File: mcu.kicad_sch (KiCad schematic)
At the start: 37 parts, among them J2 USB_C_Receptacle_USB2.0_16P, J3 Conn_01x06_Socket, SW1 SW_Push, SW2 SW_Push, SW3 SW_Rotary_1x4_MP, SW4 SW_Push_Shielded, SW5 SW_Push_Shielded, SW6 SW_Push_Shielded, SW7 SW_Push_Shielded, U1 STM32H743VITx, U6 MX25L25645GM2I

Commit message: Power Supply Speccing, IMU, Eyeballs
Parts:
- D1, D2: value LED_Filled -> QBLP601-R5-2897
- R15, R16: value R_US -> 240
- R17, R18, R19, R20: value R_US -> 5k
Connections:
- net ACCEL_CS: now also U1.32 (PC4)
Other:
- note added: "Add capacitors for hardware debounce!"
- note removed: "Use 25MHz crystal, best choice for STM32H743"
- moved on the sheet: BZ1, C1, C2, C22, C3, C4, C5, C6, C8, C9, D1, D2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

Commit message: Release Candidate 1
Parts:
- removed SW1, SW2: SW_Push, symbol Switch:SW_Push
- added C24: 4.7u, Capacitor_SMD:C_0805_2012Metric, symbol Device:C
- added D6, D9: CLV1L-FKB, LED_SMD:LED_Cree-PLCC4_3.2x2.8mm_CCW, symbol LED:CLV1L-FKB
- added D7, D8: QBLP601-R5-2897, LED_SMD:LED_0603_1608Metric, symbol Device:LED_Filled
- added J6: Conn_02x02_Counter_Clockwise, Connector_PinHeader_1.00mm:PinHeader_2x02_P1.00mm_Vertical, symbol Connector_Generic:Conn_02x02_Counter_Clockwise
- added Q3: DMG2302U, Package_TO_SOT_SMD:SOT-23, symbol Transistor_FET:DMG2302U
- added R23, R24, R30, R31: 43, Resistor_SMD:R_0805_2012Metric, symbol Device:R_US
- added R25, R29: 110, Resistor_SMD:R_0805_2012Metric, symbol Device:R_US
- added R26, R27: 240, Resistor_SMD:R_0805_2012Metric, symbol Device:R_US
- added SW1, SW2: SW_Push_Shielded, 0_airbrake_footprints:R-667766, symbol Switch:SW_Push_Shielded
- added Y1: Crystal_GND24, Crystal:Crystal_SMD_2016-4Pin_2.0x1.6mm, symbol Device:Crystal_GND24
- BZ1: footprint Buzzer_Beeper:Buzzer_TDK_PS1240P02BT_D12.2mm_H6.5mm -> 0_airbrake_footprints:CMT-322-65-SMT-TR
- C1, C2: value C -> 8p
- SW3: footprint (none) -> 0_airbrake_footprints:S-2051
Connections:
- net 3V3_MCU: now also C24.1, J6.1 (Pin_1), SW2.2
- net Buzzer_H: now also Q3.1 (G); no longer BZ1.1 (+)
- net GND: now also C24.2, D7.1 (K), D8.1 (K), J6.2 (Pin_2), Q3.2 (S), SW1.2, SW1.SH (B), SW2.SH (B), Y1.2, Y1.4
- net MCU_NRST: now also SW1.1
- net MODE_0: now also U1.81 (PD0); no longer U1.15 (PC0)
- net MODE_1: now also U1.82 (PD1); no longer U1.16 (PC1)
- net MODE_2: now also U1.83 (PD2); no longer U1.17 (PC2_C)
- net MODE_3: now also U1.84 (PD3); no longer U1.18 (PC3_C)
- net VBUS_DETECT: now also U1.51 (PB12)
- net XTAL_0: now also Y1.3
- net XTAL_1: now also Y1.1
- net STATUS1: now reaches U1.34 (PB0)
- net STATUS1: now also R27.1
- net STATUS_POW: now reaches U1.35 (PB1)
- net STATUS_POW: now also R26.1
- net BAT_OK_MCU: now reaches U1.40 (PE10)
- net STATUS0_R: now reaches U1.41 (PE11)
- net STATUS0_R: now also R25.2
- net STATUS0_G: now reaches U1.43 (PE13)
- net STATUS0_G: now also R24.2
- net STATUS0_B: now reaches U1.44 (PE14)
- net STATUS0_B: now also R23.2
- net GPS_TP: now reaches U1.47 (PB11)
- net SERVO_EN: now reaches U1.91 (PB5)
- net at R1.2, U1.94 (BOOT0): now also SW2.1
- net SERVO_SIG: now reaches U1.95 (PB8)
- net Buzzer_L: no longer names the net of U1.38 (PE8)
- net Buzzer_L: no longer BZ1.2 (-)
- net MCU_I2C1_SCL renamed EXT_I2C1_SCL
- net EXT_I2C1_SCL: now also J6.4 (Pin_4)
- net MCU_I2C1_SDA renamed EXT_I2C1_SDA
- net EXT_I2C1_SDA: now also J6.3 (Pin_3)
- net MCU_I2C3_SCL renamed BME680_I2C3_SCL
- net MCU_I2C3_SDA renamed BME680_I2C3_SDA
- new net: D9.2 (RK), R29.1
- new net: D9.3 (GK), R30.1
- new net: D9.4 (BK), R31.1
- new net: BZ1.2 (-), Q3.3 (D)
- new net: D8.2 (A), R27.2
- new net: D6.2 (RK), R25.1
- new net: D7.2 (A), R26.2
- new net: D6.3 (GK), R24.1
- new net: D6.4 (BK), R23.1
- new net 3V6_SWITCHING: BZ1.1 (+), D6.1 (A), D9.1 (A)
- new net STATUS1_B: R31.2, U1.17 (PC2_C)
- new net STATUS1_G: R30.2, U1.16 (PC1)
- new net STATUS1_R: R29.2, U1.15 (PC0)
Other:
- note added: "5V Tolerant!"
- note added: "External I2C"
- note added: "https://www.digikey.com/en/products/detail/cree-led/CLV1L-FKB-CJQRNQEFGBB79353/9659628"
- note removed: "Add capacitors for hardware debounce!"
- note removed: "Run buzzer on complementary PWM to make it really loud!"
- moved on the sheet: BZ1, C1, C2, SW3, SW4, SW5, SW6, SW7

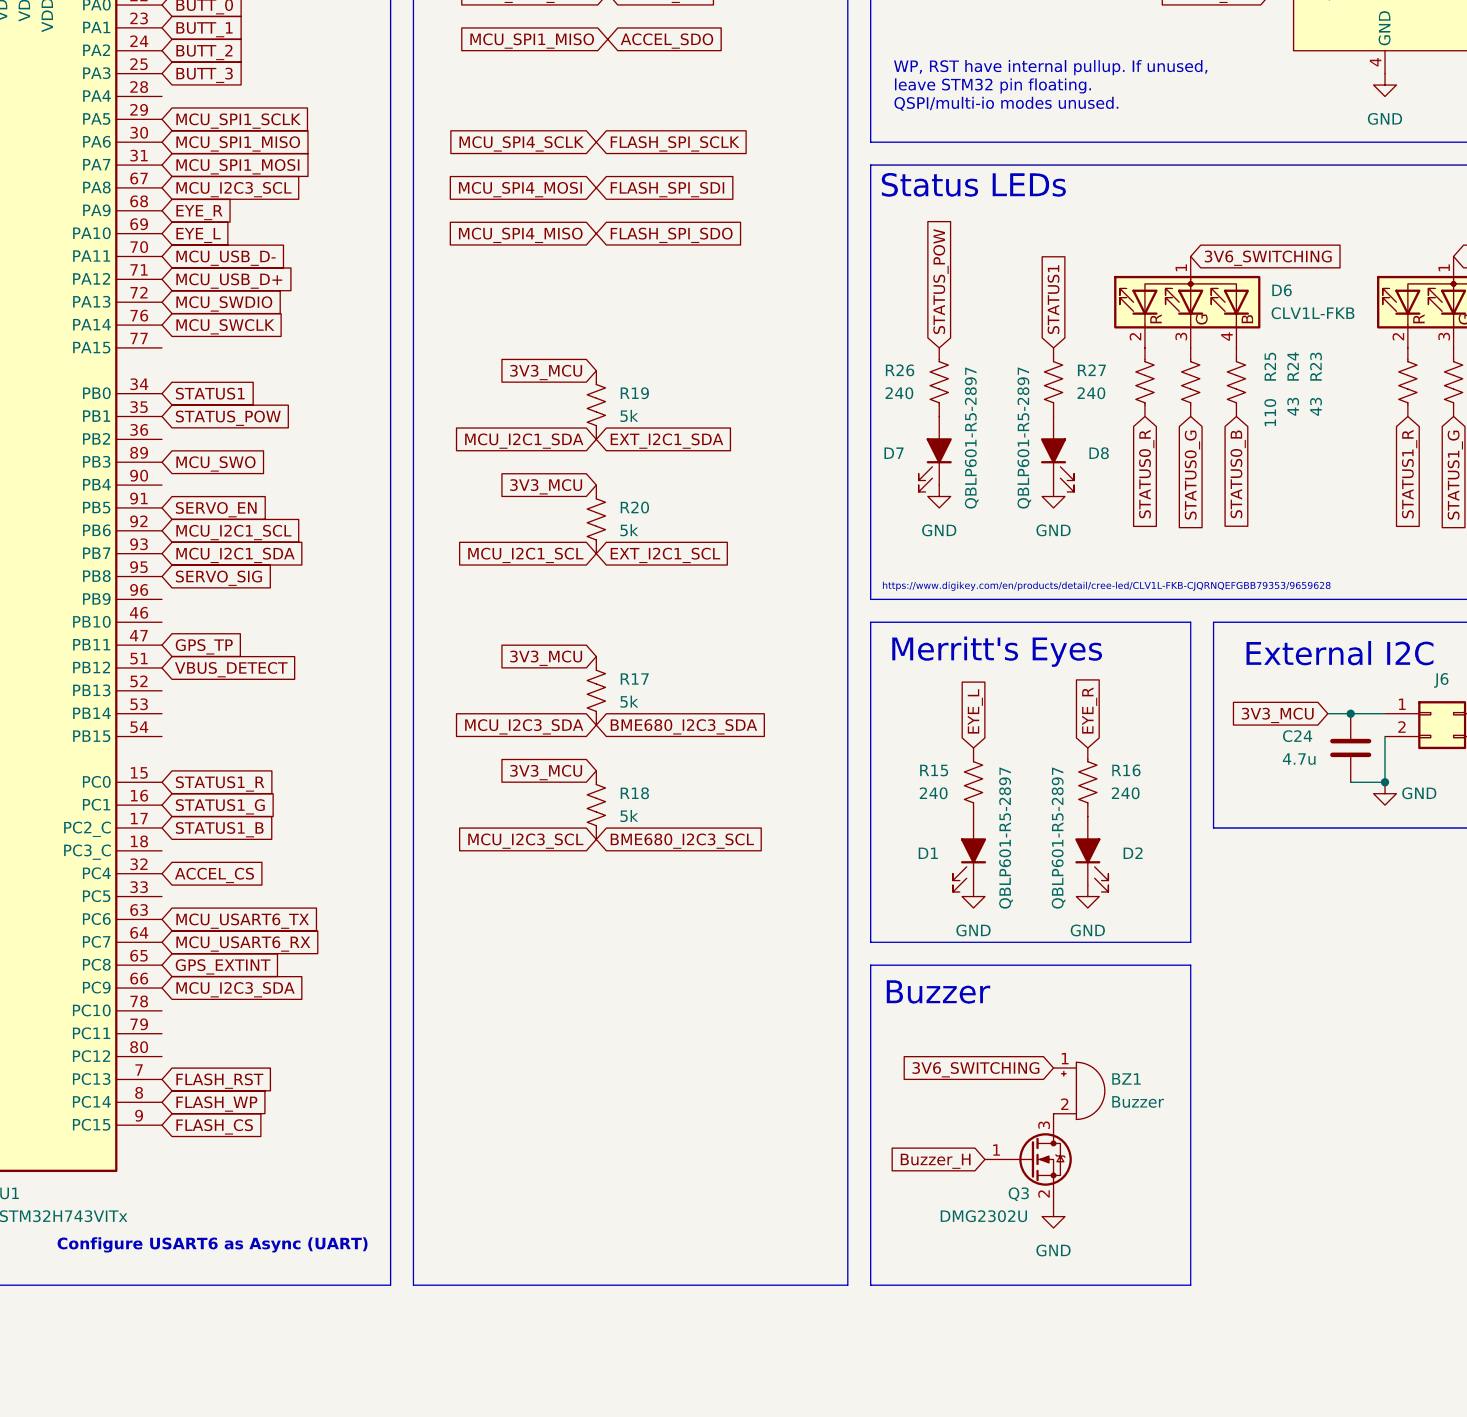
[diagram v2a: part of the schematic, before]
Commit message: Release Candidate 2
Incorporates fixes for all identified issues in the PCBR
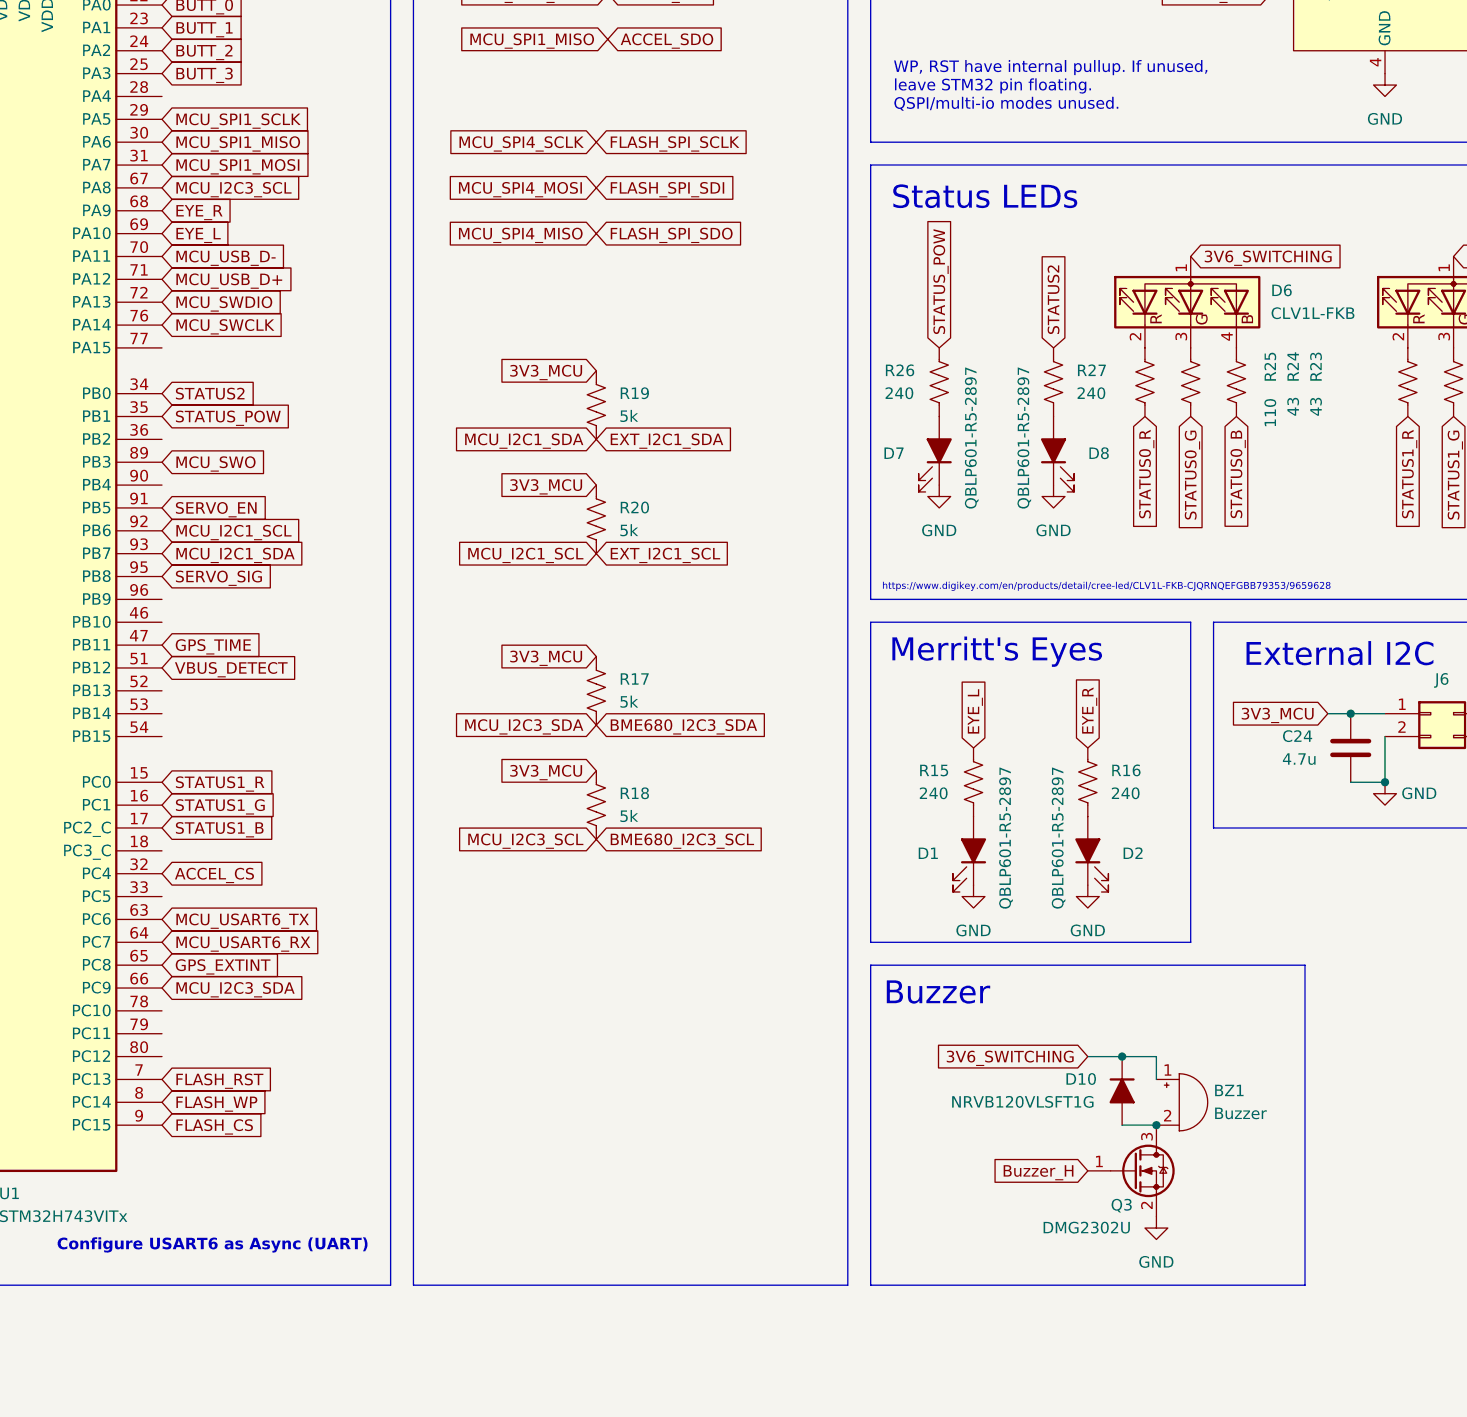
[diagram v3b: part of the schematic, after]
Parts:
- added D10: NRVB120VLSFT1G, Diode_SMD:D_SOD-123F, symbol Device:D_Filled
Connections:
- net 3V6_SWITCHING: now also D10.1 (K)
- net at BZ1.2 (-), Q3.3 (D): now also D10.2 (A)
- net GPS_TP renamed GPS_TIME
- net STATUS1 renamed STATUS2
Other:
- moved on the sheet: BZ1, Q3
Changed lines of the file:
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@@
 	)
 	(junction
+		(at 325.12 184.15)
+		(diameter 0)
+		(color 0 0 0 0)
+	)
+	(junction
 		(at 199.39 52.07)
 		(diameter 0)
 		(color 0 0 0 0)
 	)
+	(junction
+		(at 321.31 176.53)
+		(diameter 0)
+		(color 0 0 0 0)
+	)
 	(no_connect
 		(at 171.45 69.85)
@@
 	(wire
 		(pts
+			(xy 325.12 176.53) (xy 325.12 179.07)
+		)
+		(stroke
+			(width 0)
+			(type default)
+		)
+	)
+	(wire
+		(pts
 			(xy 74.93 93.98) (xy 82.55 93.98)
 		)
@@
 	(wire
 		(pts
+			(xy 321.31 184.15) (xy 325.12 184.15)
+		)
+		(stroke
+			(width 0)
+			(type default)
+		)
+	)
+	(wire
+		(pts
 			(xy 74.93 101.6) (xy 82.55 101.6)
 		)
@@
 	(wire
 		(pts
+			(xy 317.5 176.53) (xy 321.31 176.53)
+		)
+		(stroke
+			(width 0)
+			(type default)
+		)
+	)
+	(wire
+		(pts
 			(xy 346.71 138.43) (xy 350.52 138.43)
 		)
@@
 	(wire
 		(pts
+			(xy 321.31 176.53) (xy 325.12 176.53)
+		)
+		(stroke
+			(width 0)
+			(type default)
+		)
+	)
+	(wire
+		(pts
 			(xy 139.7 64.77) (xy 146.05 64.77)
 		)
@@
 	(rectangle
 		(start 293.37 166.37)
-		(end 328.93 201.93)
+		(end 341.63 201.93)
 		(stroke
 			(width 0)
@@
 	(text "Status LEDs"
 		(exclude_from_sim no)
-		(at 304.8 80.01 0)
+		(at 306.07 81.28 0)
 		(effects
 			(font
@@
 		)
 	)
-	(global_label "STATUS1"
+	(global_label "STATUS2"
 		(shape input)
 		(at 313.69 97.79 90)
@@
 		)
 	)
-	(global_label "GPS_TP"
-		(shape input)
-		(at 214.63 130.81 0)
-		(fields_autoplaced yes)
-		(effects
-			(font
-				(size 1.27 1.27)
-			)
-			(justify left)
-		)
-		(property "Intersheetrefs" "${INTERSHEET_REFS}"
-			(at 224.5699 130.81 0)
-			(effects
-				(font
-					(size 1.27 1.27)
-				)
-				(justify left)
-				(hide yes)
-			)
-		)
-	)
 	(global_label "XTAL_1"
 		(shape input)
@@
 		)
 	)
+	(global_label "GPS_TIME"
+		(shape input)
+		(at 214.63 130.81 0)
+		(fields_autoplaced yes)
+		(effects
+			(font
+				(size 1.27 1.27)
+			)
+			(justify left)
+		)
+		(property "Intersheetrefs" "${INTERSHEET_REFS}"
+			(at 226.5051 130.81 0)
+			(effects
+				(font
+					(size 1.27 1.27)
+				)
+				(justify left)
+				(hide yes)
+			)
+		)
+	)
 	(global_label "3V3_MCU"
 		(shape input)
@@
 	(global_label "3V6_SWITCHING"
 		(shape input)
-		(at 313.69 177.8 180)
+		(at 317.5 176.53 180)
 		(fields_autoplaced yes)
 		(effects
@@
 		)
 		(property "Intersheetrefs" "${INTERSHEET_REFS}"
-			(at 296.1905 177.8 0)
+			(at 300.0005 176.53 0)
 			(effects
 				(font
@@
 		)
 	)
-	(global_label "STATUS1"
+	(global_label "STATUS2"
 		(shape input)
 		(at 214.63 102.87 0)
@@
 	(global_label "Buzzer_H"
 		(shape input)
-		(at 306.07 187.96 180)
+		(at 317.5 189.23 180)
 		(fields_autoplaced yes)
 		(effects
@@
 		)
 		(property "Intersheetrefs" "${INTERSHEET_REFS}"
-			(at 294.4367 187.96 0)
+			(at 305.8667 189.23 0)
 			(effects
 				(font
@@
 	(symbol
 		(lib_id "Transistor_FET:DMG2302U")
-		(at 311.15 187.96 0)
+		(at 322.58 189.23 0)
 		(unit 1)
 		(exclude_from_sim no)
@@
 		(dnp no)
 		(property "Reference" "Q3"
-			(at 308.61 191.77 0)
+			(at 320.04 193.04 0)
 			(effects
 				(font
@@
 		)
 		(property "Value" "DMG2302U"
-			(at 300.99 194.31 0)
+			(at 312.42 195.58 0)
 			(effects
 				(font
@@
 		)
 		(property "Footprint" "Package_TO_SOT_SMD:SOT-23"
-			(at 316.23 189.865 0)
+			(at 327.66 191.135 0)
 			(effects
 				(font
@@
 		)
 		(property "Datasheet" "http://www.diodes.com/assets/Datasheets/DMG2302U.pdf"
-			(at 316.23 191.77 0)
+			(at 327.66 193.04 0)
 			(effects
 				(font
@@
 		)
 		(property "Description" "4.2A Id, 20V Vds, N-Channel MOSFET, SOT-23"
-			(at 311.15 187.96 0)
+			(at 322.58 189.23 0)
 			(effects
 				(font
@@
 	(symbol
 		(lib_id "Device:Buzzer")
-		(at 316.23 180.34 0)
+		(at 327.66 181.61 0)
 		(unit 1)
 		(exclude_from_sim no)
@@
 		(fields_autoplaced yes)
 		(property "Reference" "BZ1"
-			(at 320.04 179.0699 0)
+			(at 331.47 180.3399 0)
 			(effects
 				(font
@@
 		)
 		(property "Value" "Buzzer"
-			(at 320.04 181.6099 0)
+			(at 331.47 182.8799 0)
 			(effects
 				(font
@@
 		)
 		(property "Footprint" "0_airbrake_footprints:CMT-322-65-SMT-TR"
-			(at 315.595 177.8 90)
+			(at 327.025 179.07 90)
 			(effects
 				(font
@@
 		)
 		(property "Datasheet" "~"
-			(at 315.595 177.8 90)
+			(at 327.025 179.07 90)
 			(effects
 				(font
@@
 		)
 		(property "Description" "Buzzer, polarized"
-			(at 316.23 180.34 0)
+			(at 327.66 181.61 0)
 			(effects
 				(font
@@
 	)
 	(symbol
+		(lib_id "Device:D_Filled")
+		(at 321.31 180.34 270)
+		(unit 1)
+		(exclude_from_sim no)
+		(in_bom yes)
+		(on_board yes)
+		(dnp no)
+		(property "Reference" "D10"
+			(at 314.96 179.07 90)
+			(effects
+				(font
+					(size 1.27 1.27)
+				)
+				(justify left)
+			)
+		)
+		(property "Value" "NRVB120VLSFT1G"
+			(at 302.26 181.61 90)
+			(effects
+				(font
+					(size 1.27 1.27)
+				)
+				(justify left)
+			)
+		)
+		(property "Footprint" "Diode_SMD:D_SOD-123F"
+			(at 321.31 180.34 0)
+			(effects
+				(font
+					(size 1.27 1.27)
+				)
+				(hide yes)
+			)
+		)
+		(property "Datasheet" "~"
+			(at 321.31 180.34 0)
+			(effects
+				(font
+					(size 1.27 1.27)
+				)
+				(hide yes)
+			)
+		)
+		(property "Description" "Diode, filled shape"
+			(at 321.31 180.34 0)
+			(effects
+				(font
+					(size 1.27 1.27)
+				)
+				(hide yes)
+			)
+		)
+		(property "Sim.Device" "D"
+			(at 321.31 180.34 0)
+			(effects
+				(font
+					(size 1.27 1.27)
+				)
+				(hide yes)
+			)
+		)
+		(property "Sim.Pins" "1=K 2=A"
+			(at 321.31 180.34 0)
+			(effects
+				(font
+					(size 1.27 1.27)
+				)
+				(hide yes)
+			)
+		)
+		(pin "1"
+		)
+		(pin "2"
+		)
+		(instances
+			(project "airbrake_mod"
+				(path "/b8365613-e621-4ec6-998b-f60341596878/1da62f80-fb6d-4565-8f94-99dca1874ea1"
+					(reference "D10")
+					(unit 1)
+				)
+			)
+		)
+	)
+	(symbol
 		(lib_id "Device:R_US")
 		(at 300.99 101.6 0)
@@
 	(symbol
 		(lib_id "power:GND")
-		(at 313.69 193.04 0)
+		(at 325.12 194.31 0)
 		(unit 1)
 		(exclude_from_sim no)
@@
 		(fields_autoplaced yes)
 		(property "Reference" "#PWR068"
-			(at 313.69 199.39 0)
+			(at 325.12 200.66 0)
 			(effects
 				(font
@@
 		)
 		(property "Value" "GND"
-			(at 313.69 198.12 0)
+			(at 325.12 199.39 0)
 			(effects
 				(font
@@
 		)
 		(property "Footprint" ""
-			(at 313.69 193.04 0)
+			(at 325.12 194.31 0)
 			(effects
 				(font
@@
 		)
 		(property "Datasheet" ""
-			(at 313.69 193.04 0)
+			(at 325.12 194.31 0)
 			(effects
 				(font
@@
 		)
 		(property "Description" "Power symbol creates a global label with name \"GND\" , ground"
-			(at 313.69 193.04 0)
+			(at 325.12 194.31 0)
 			(effects
 				(font

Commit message: Release Candidate 3
Fixed name, one location with vias. Added production files in prep for merge request.
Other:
- title: Airbrakes PCB - Earendel -> Airbrakes PCB - Veðrfölnir 
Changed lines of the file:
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@@
 	(paper "B")
 	(title_block
-		(title "Airbrakes PCB - Earendel")
+		(title "Airbrakes PCB - Veðrfölnir ")
 		(date "2025-02-18")
 		(rev "v2025.01A")
